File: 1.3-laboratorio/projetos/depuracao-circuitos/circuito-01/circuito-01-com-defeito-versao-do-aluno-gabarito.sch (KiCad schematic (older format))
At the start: 22 parts, among them J1 Conn_01x07_Male, J2 Conn_01x07_Male, J3 Conn_01x07_Male, J4 Conn_01x07_Male, J5 Conn_01x07_Male, J6 Conn_01x07_Male, J7 Conn_01x05, J8 Conn_01x05, P1 CONN_01X02, SW1 SW_DIP_x04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

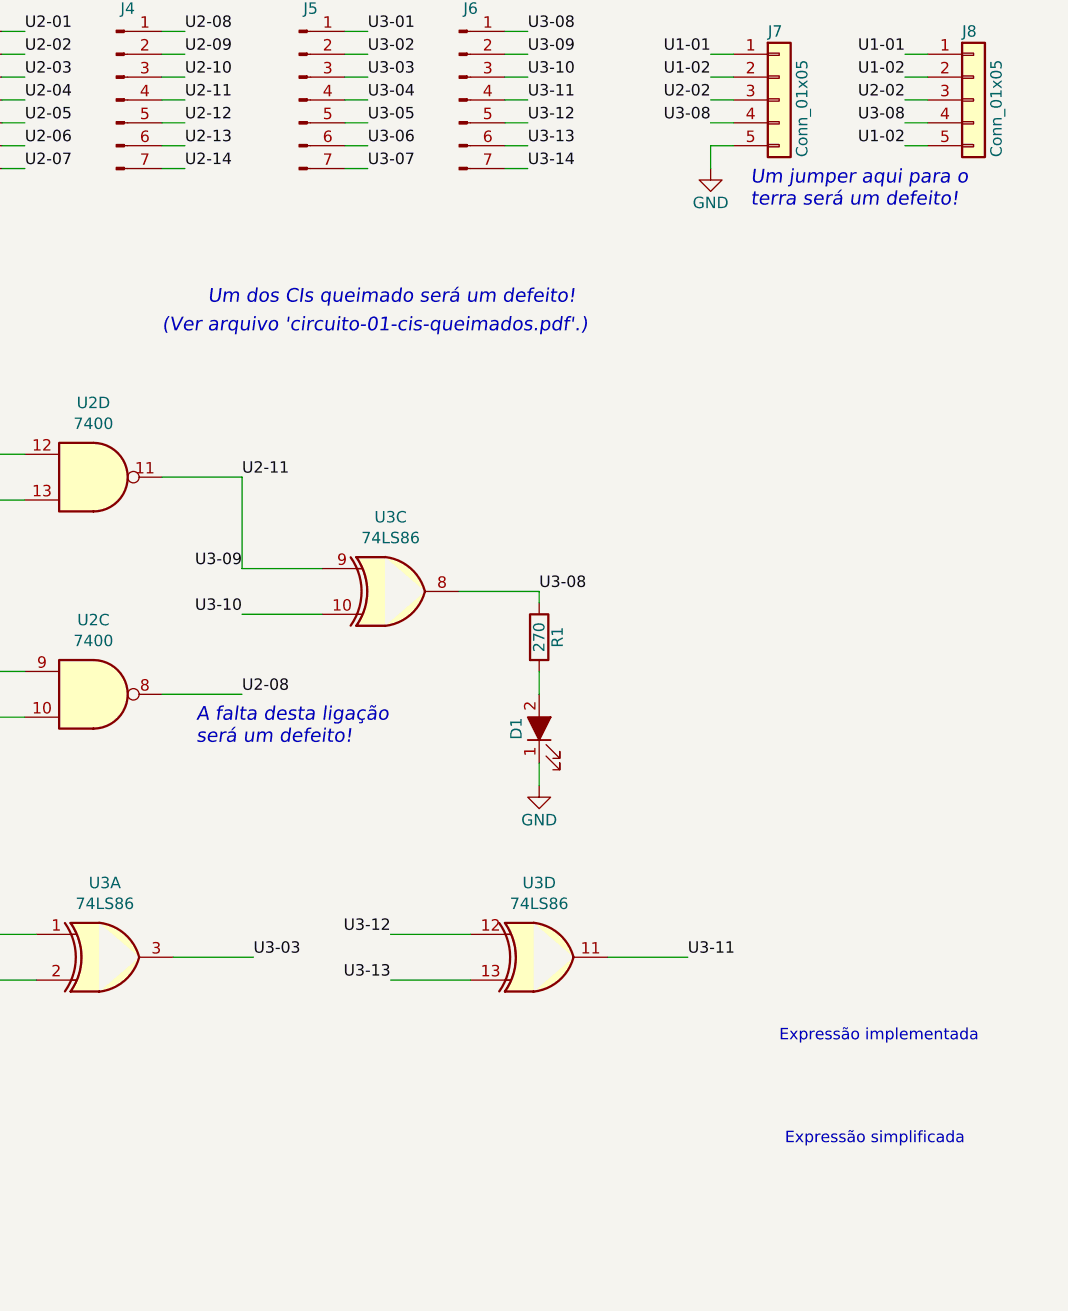
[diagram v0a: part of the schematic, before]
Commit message: Criação do subdiretório 'pdf' e das versões para professor e para aluno do Circuito para Depuração 01.
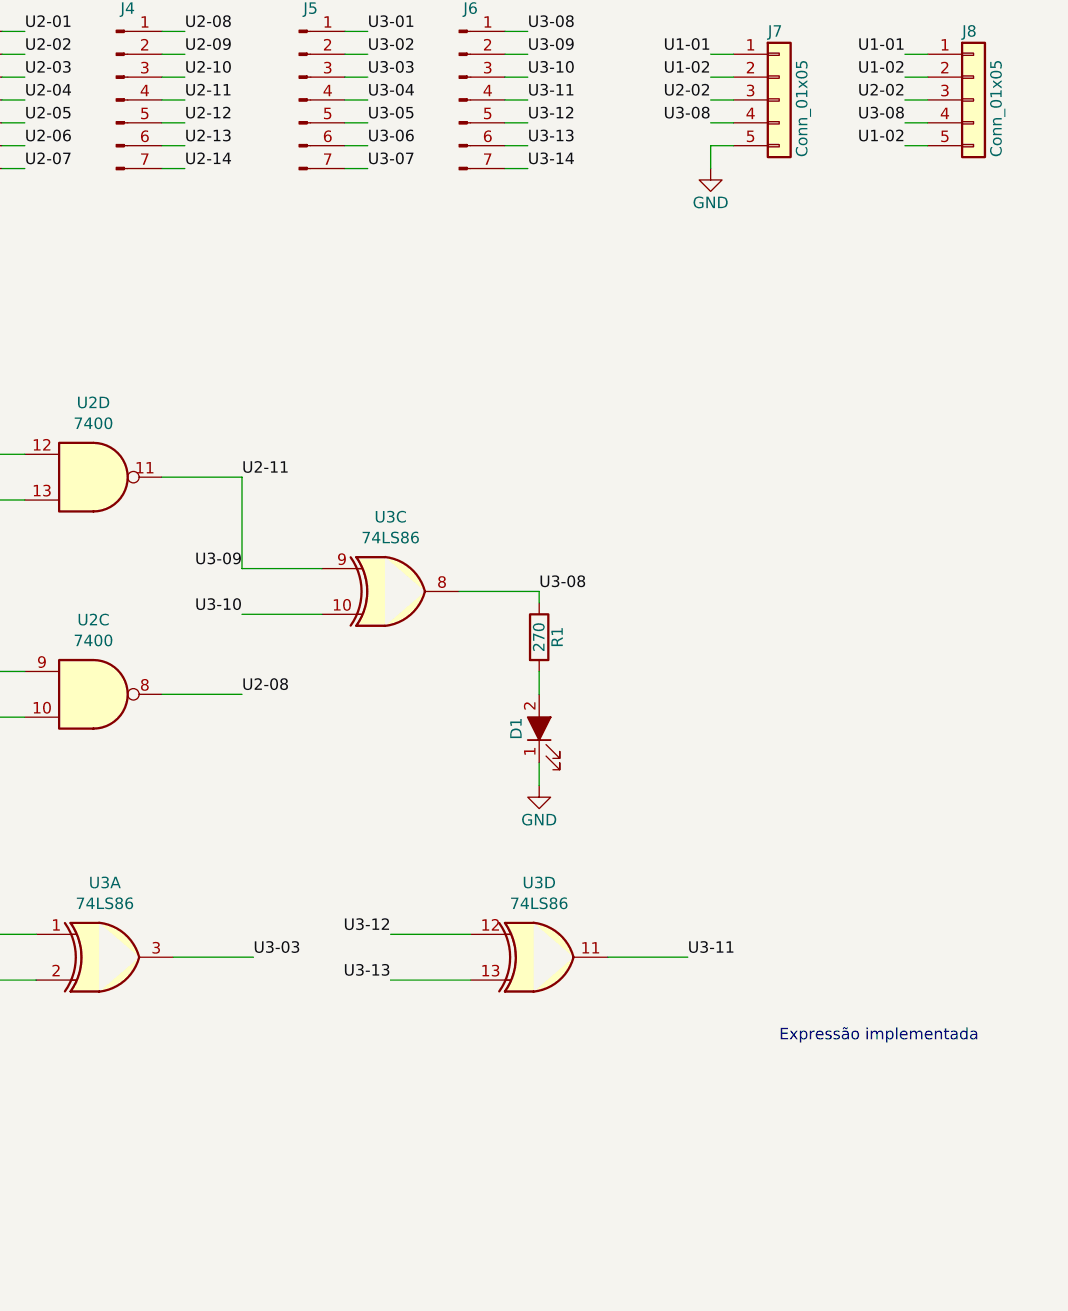
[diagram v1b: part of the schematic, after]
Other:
- note removed: "(Ver arquivo 'circuito-01-cis-queimados.pdf'.)"
- note removed: "A falta desta ligação\nserá um defeito!"
- note removed: "Expressão simplificada"
- note removed: "Um dos CIs queimado será um defeito!"
- note removed: "Um jumper aqui para o\nterra será um defeito!"
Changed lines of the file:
@@
 Comment2 "Com defeitos propositais."
 Comment3 ""
-Comment4 "(Base para a PCI e para gerar as versões do professor e do aluno.)"
+Comment4 "(VERSÃO DO ALUNO - GABARITO)"
 $EndDescr
 $Comp
@@
 Wire Wire Line
 	2050 3450 2300 3450
-Text Notes 9225 1925 0    60   Italic 0
-Um jumper aqui para o\nterra será um defeito!
-Text Notes 6800 4275 0    60   Italic 0
-A falta desta ligação\nserá um defeito!
-Text Notes 6850 2350 0    60   Italic 0
-Um dos CIs queimado será um defeito!
 Wire Wire Line
 	9900 1650 10000 1650
@@
 EndData
 $EndBitmap
-$Bitmap
-Pos 9825 6125
-Scale 1.000000
-Data
-89 50 4E 47 0D 0A 1A 0A 00 00 00 0D 49 48 44 52 00 00 00 CC 00 00 00 2F 08 02 00 00 00 20 90 B2
-89 00 00 00 03 73 42 49 54 08 08 08 DB E1 4F E0 00 00 0B 0C 49 44 41 54 78 9C ED 9B 7D 4C 13 F7
-1F C7 3F ED AE 82 4C 79 52 64 22 62 05 5D 5C 83 E0 44 A9 50 1F 20 46 29 A0 82 D9 E6 A6 89 64 A8
-34 73 6A 1C C6 87 19 74 A0 84 3D 24 84 36 9A FD 33 D1 49 08 83 2D 8A 1A 2D 81 29 3E 41 A7 A0 62
-16 8D 1A 85 02 0E 1C 5A DA 6A 6B E1 DA 5E EF F6 C7 6D AC E9 5D CB 5D CB C1 CF DF EE F5 E7 F7 F3
-7D 78 03 EF FB 7E 3E DF EF 1D 02 82 20 80 87 87 4B 84 63 2D 80 E7 FF 1F DE 64 3C 9C C3 9B 8C 87
-73 78 93 F1 70 0E 6F 32 1E CE E1 4D C6 C3 39 BC C9 78 38 87 37 19 0F E7 F0 26 E3 E1 1C DE 64 3C
-9C F3 86 99 AC A8 A8 48 F0 DF A6 A8 A8 68 AC FF 08 AC 11 F0 EF 2E 79 B8 E6 0D DB C9 78 DE 44 10
-86 FD AC 56 6B 4B 4B 4B 6F 6F EF A4 49 93 64 32 D9 DB 6F BF 0D 00 76 BB BD A7 A7 67 E6 CC 99 5C
-2A F4 9E 9A 9A 9A E9 D3 A7 CB 64 B2 B1 16 F2 5F 67 F8 74 89 E3 78 59 59 59 75 75 B5 54 2A 95 48
-24 9D 9D 9D 4D 4D 4D 9F 7D F6 D9 A6 4D 9B B6 6E DD 9A 96 96 96 9D 9D 3D 3A 5A 59 D1 D5 D5 25 91
-48 F2 F3 F3 4B 4A 4A C6 5A 8B 5B 8C 46 E3 AA 55 AB 6C 36 1B 6D 14 41 90 77 DE 79 67 E9 D2 A5 B9
-B9 B9 C1 C1 C1 A3 AC CD 19 93 C9 94 91 91 61 B5 5A 69 A3 22 91 28 3A 3A 7A EE DC B9 0A 85 22 24
-24 84 A6 07 E1 91 E7 CF 9F 2F 59 B2 A4 A0 A0 C0 6A B5 0E 35 A2 28 BA 71 E3 C6 BC BC 3C 81 40 D0
-DF DF EF 79 86 B1 22 2B 2B 0B 00 72 73 73 C7 5A C8 30 E0 38 DE DF DF 4F FE 6D 4E 9E 3C 89 E3 38
-D9 8E 61 58 7B 7B 7B 55 55 D5 AC 59 B3 66 CC 98 A1 D1 68 C6 5C A7 C1 60 08 0F 0F 07 80 D3 A7 4F
-0F E9 24 08 C2 6C 36 D7 D7 D7 47 44 44 04 05 05 35 34 34 50 C7 7A 32 19 8E E3 2B 57 AE FC F2 CB
-2F A9 21 BD 5E 1F 14 14 34 77 EE 5C DF D5 73 41 5D 5D DD D4 A9 53 01 20 3D 3D 7D A4 E6 B4 D9 6C
-23 35 95 0B 46 A3 51 28 14 8A 44 22 8B C5 42 8D 5A AD D6 94 94 14 04 41 6E DE BC C9 91 00 86 BC
-7E FD 5A 24 12 4D 98 30 C1 6E B7 53 A3 6D 6D 6D 00 10 1C 1C 4C DD 77 3C 99 4C A5 52 4D 9B 36 CD
-DD 2F 37 2D 2D 6D DB B6 6D 5E 2B E6 0E 14 45 D3 D2 D2 BE FF FE 7B 00 98 37 6F 9E 2F 53 BD 7C F9
-52 A5 52 65 67 67 AF 5D BB 36 2A 2A 2A 3B 3B 3B 23 23 23 3F 3F FF EE DD BB 23 A5 96 20 88 73 E7
-CE 01 C0 E2 C5 8B DD 75 E8 EC EC 0C 08 08 48 4A 4A F2 62 72 87 C3 F1 F1 C7 1F FB A0 EE 5F 1A 1A
-1A 00 40 2E 97 BB EB 10 1D 1D 0D 00 B5 B5 B5 2E ED 9E 4E 97 47 8E 1C 49 49 49 11 89 44 B4 51 B1
-58 BC 6C D9 32 C6 69 7D F4 28 2D 2D DD BE 7D 7B 4C 4C 0C 00 FC F9 E7 9F 5E CF 73 EC D8 B1 F4 F4
-F4 E8 E8 E8 5F 7E F9 A5 B6 B6 36 39 39 B9 A6 A6 46 AD 56 6F D9 B2 45 A9 54 6E DC B8 F1 D5 AB 57
-23 22 F8 EA D5 AB 00 90 92 92 E2 AE 83 58 2C 4E 48 48 B8 71 E3 46 63 63 23 DB C9 07 07 07 4F 9F
-3E ED 83 BA 7F F1 AC 93 CC FB 00 80 20 AE A7 49 B7 26 33 99 4C 5A AD 36 20 20 C0 5D 07 AB D5 BA
-74 E9 52 F6 52 B9 E5 E9 D3 A7 F7 EE DD 5B B5 6A 55 44 44 04 00 E8 74 3A 0C C3 D8 4E 42 10 C4 B6
-6D DB 1E 3E 7C D8 D8 D8 B8 7A F5 6A 97 C7 4C 22 91 54 54 54 7C F4 D1 47 59 59 59 DD DD DD BE 6B
-BE 72 E5 0A 78 34 19 00 C4 C6 C6 02 C0 EF BF FF EE FB 72 5E E3 59 67 4B 4B 8B C9 64 1A 37 6E 1C
-CD D6 E3 6E EB 1B 1C 1C 14 0A 85 91 91 91 26 93 89 B6 C3 98 97 08 B4 6C D8 B0 A1 A3 A3 83 20 08
-F2 A9 02 80 DE DE 5E B6 93 14 16 16 96 95 95 B9 34 7E F2 C9 27 28 8A 3A B7 74 76 76 CA 64 32 B3
-D9 EC 8B 60 83 C1 E0 A1 20 1B A2 B8 B8 18 00 F2 F2 F2 D8 CE FF FA F5 6B 04 41 7C 10 F8 37 66 B3
-19 41 10 77 05 99 D5 6A 8D 8F 8F 07 80 F2 F2 72 6A D4 ED 4E E6 EF EF BF 70 E1 C2 9E 9E 9E E5 CB
-97 D7 D7 D7 53 8F AF 52 A9 D4 BB 07 82 3B 7E FD F5 D7 77 DF 7D 97 AC 0C 26 4D 9A E4 E7 E7 07 EC
-33 E6 DD BB 77 7F FB ED B7 2F BE F8 62 D8 9E 62 B1 58 A1 50 14 16 16 7A A7 96 E4 FA F5 EB 38 8E
-4B A5 52 0F 49 03 00 74 3A 1D 00 98 4C 26 5F D6 F2 05 8D 46 83 61 D8 E2 C5 8B A9 D9 50 A7 D3 AD
-5B B7 EE F1 E3 C7 2A 95 6A F3 E6 CD D4 B1 9E 6A 32 95 4A 35 61 C2 84 5B B7 6E A5 A7 A7 87 84 84
-C8 E5 F2 B2 B2 B2 11 49 10 5C 60 B3 D9 94 4A E5 BE 7D FB 86 5A C8 03 26 5B 93 7D FD F5 D7 3F FE
-F8 A3 40 20 60 D2 39 27 27 E7 E9 D3 A7 CF 9E 3D 63 B5 84 33 C3 16 64 24 F7 EF DF 07 80 C8 C8 48
-AF 17 F2 11 52 A7 54 2A B5 FC C3 F3 E7 CF 2F 5E BC 58 52 52 92 92 92 12 16 16 76 FF FE FD 9D 3B
-77 D2 8E F5 74 E3 BF 68 D1 A2 96 96 96 E2 E2 62 B5 5A 6D 36 9B 1B 1A 1A 1A 1A 1A F6 EF DF 5F 52
-52 B2 7B F7 6E 26 CA 4E 9D 3A A5 50 28 08 36 AF 47 85 42 61 4D 4D CD 8A 15 2B 98 0F 21 29 2B 2B
-FB FC F3 CF FD FD FD 87 5A 22 22 22 BA BA BA 58 99 CC 60 30 F8 F9 F9 4D 9B 36 8D F9 90 DC DC DC
-DA DA DA ED DB B7 B3 D0 EA 04 93 82 8C 20 88 3B 77 EE 00 C0 EC D9 B3 BD 5B C5 77 48 9D 46 A3 B1
-B4 B4 74 A8 D1 6A B5 B6 B7 B7 27 24 24 C8 E5 72 32 81 D0 C3 24 1F DB ED F6 E6 E6 E6 A2 A2 A2 B8
-B8 38 72 54 5D 5D 1D 93 81 38 8E EB F5 FA 7E 36 18 0C 06 E7 8B 3E 86 FC F1 C7 1F D4 83 FA 87 1F
-7E 08 00 87 0E 1D 62 3E CF 99 33 67 68 AB 0A 82 AE 26 23 41 51 F4 83 0F 3E 60 BE 84 33 7A BD 5E
-20 10 0C 5B 90 91 0E 13 08 04 3D 3D 3D 6C 97 18 91 9A 8C 2C C8 02 03 03 31 0C A3 46 2F 5C B8 80
-20 88 5C 2E 77 77 DB C5 E8 DD 25 82 20 32 99 4C 26 93 7D F5 D5 57 05 05 05 DF 7C F3 4D 45 45 45
-7A 7A FA B0 03 05 02 41 68 68 28 93 25 7C 64 D7 AE 5D 32 99 4C AD 56 3B 37 0E 0C 0C 00 CB 74 D9
-D3 D3 83 E3 B8 46 A3 A1 86 74 3A 9D 46 A3 21 EB 3C 17 50 14 65 A9 F7 6F AE 5F BF 4E 10 C4 B0 05
-59 65 65 25 00 24 27 27 7B D8 62 9F 3D 7B 76 E9 D2 25 82 92 34 50 14 C5 71 BC A2 A2 82 3A 44 28
-14 CA E5 F2 B0 B0 B0 61 75 36 37 37 63 18 B6 64 C9 92 B7 DE 7A 8B 1A CD CC CC 5C BF 7E 7D 65 65
-E5 E1 C3 87 C9 03 8A 0B F4 26 7B F1 E2 C5 94 29 53 A8 ED 02 81 E0 F0 E1 C3 2A 95 EA D1 A3 47 C3
-2A 1B 35 1A 1B 1B 31 0C 7B F9 F2 E5 ED DB B7 9D DB C9 CB 0B 56 26 B3 D9 6C 1D 1D 1D 76 BB 9D 1A
-D2 EB F5 AD AD AD B4 B7 86 16 8B 85 A5 E4 BF 61 52 90 61 18 56 5D 5D 0D 00 87 0E 1D F2 D0 AD B3
-B3 93 D6 64 E4 61 F0 D2 A5 4B D4 21 42 A1 30 36 36 96 89 C9 48 9D 1E AE 45 93 93 93 2B 2B 2B CF
-9F 3F 4F 6B 32 9A 74 A9 D5 6A 0B 0B 0B 3D 6C 9E 71 71 71 32 99 8C F5 9E CB 0D 36 9B 4D 2E 97 0F
-0C 0C 50 43 E5 E5 E5 00 90 98 98 C8 7C B6 9F 7E FA A9 AA AA 8A 36 E4 2E 5D 62 18 96 95 95 C5 7C
-09 67 C8 F2 83 34 87 3B BE FB EE 3B F0 E1 FD D8 88 A4 CB C4 C4 44 00 68 6D 6D 75 D7 61 EF DE BD
-00 20 16 8B 69 A3 34 3B D9 D5 AB 57 A3 A2 A2 DC 79 D6 E1 70 74 74 74 30 AC 73 D5 6A F5 C1 83 07
-09 96 85 BF 52 A9 64 7E CD AB 54 2A B7 6E DD 3A 7E FC 78 6A 88 FC 29 58 ED 64 89 89 89 2A 95 6A
-C3 86 0D CC 87 B4 B5 B5 CD 9B 37 8F 79 FF 21 F4 7A FD BD 7B F7 44 22 51 52 52 92 BB 3E 4F 9E 3C
-29 2C 2C 8C 8C 8C A4 CD 77 A3 83 D9 6C BE 73 E7 CE C4 89 13 E7 CF 9F EF AE 4F 53 53 13 00 A4 A6
-A6 D2 46 E9 4D E6 21 F7 37 37 37 13 04 91 97 97 C7 44 5F 6A 6A 2A 59 47 33 E9 4C 22 14 0A 25 12
-09 C3 CE BD BD BD 6D 6D 6D E4 63 44 85 3C F0 F7 F5 F5 11 04 C1 F0 4A 22 26 26 E6 C9 93 27 28 8A
-3A 9F 52 3D 53 59 59 49 7B 39 34 2C C3 16 64 16 8B 25 27 27 27 20 20 E0 EC D9 B3 4C 92 1A 47 34
-37 37 3B 1C 0E 99 4C 46 5B 90 01 C0 CF 3F FF 7C E3 C6 8D D0 D0 D0 03 07 0E D0 4F 41 DD DC A2 A2
-A2 16 2D 5A 44 BB EF A1 28 FA DE 7B EF 1D 3D 7A 94 F5 86 CB 0D 99 99 99 8F 1F 3F 76 17 35 1A 8D
-E4 CF C8 EA 7B A4 53 A7 4E ED DC B9 93 DA 4E 9B 2E 6F DE BC E9 F5 D1 72 C7 8E 1D 00 70 E0 C0 01
-DA A8 56 AB 95 4A A5 33 66 CC 78 F0 E0 81 77 F3 93 F8 9E 2E F7 EC D9 03 00 DF 7E FB 2D 6D B4 B5
-B5 35 34 34 14 41 90 C6 C6 46 77 33 B8 9A 4C AB D5 02 80 54 2A DD BF 7F BF 4B 48 A7 D3 65 64 64
-E4 E6 E6 7A 71 C5 30 E2 18 8D C6 4F 3F FD D4 DF DF DF 60 30 B8 EB D3 DE DE 4E 9A CC 73 D1 43 65
-CD 9A 35 D4 EF A2 A8 26 33 9B CD 0B 17 2E 24 DF 62 B1 C5 62 B1 90 DF 66 A9 D5 6A E7 76 1C C7 1F
-3D 7A 94 9F 9F 1F 14 14 B4 63 C7 8E 57 AF 5E 79 31 B9 33 3E 9A 6C 70 70 90 4C 6B 4D 4D 4D 2E A1
-F6 F6 F6 82 82 02 04 41 DE 7F FF 7D CF 9F BB B9 9A EC C4 89 13 39 39 39 18 86 ED D9 B3 67 FE FC
-F9 2A 95 AA AE AE EE EC D9 B3 FB F6 ED 9B 33 67 8E BB A2 78 34 C1 71 7C D9 B2 65 21 21 21 81 81
-81 E3 C7 8F 0F 0D 0D 25 33 B8 33 17 2F 5E 8C 8F 8F 0F 0B 0B 0B 0E 0E 0E 0C 0C 0C 0F 0F 5F B0 60
-C1 B5 6B D7 18 2E 61 32 99 E4 72 F9 B9 73 E7 9C 1B 5D 4C D6 DD DD 9D 99 99 E9 E1 F1 75 47 69 69
-69 5C 5C DC D0 97 AE 62 B1 78 C1 3F C4 C6 C6 CE 9C 39 33 29 29 A9 B8 B8 B8 AB AB 8B ED CC B4 78
-6D B2 23 47 8E C4 C7 C7 0F 7D E9 1A 13 13 33 A4 33 21 21 61 F2 E4 C9 E1 E1 E1 72 B9 FC F8 F1 E3
-0E 87 C3 F3 54 AE 9F 5F 5F BE 7C 39 29 29 89 AC A3 FB FA FA CE 9F 3F DF DD DD ED 70 38 24 12 C9
-9A 35 6B 82 82 82 7C 48 EE 6F 12 03 03 03 0A 85 42 20 10 28 95 CA C9 93 27 03 C0 FA F5 EB 4F 9E
-3C E9 E7 E7 E7 70 38 CA CB CB 7F F8 E1 87 E3 C7 8F 7B 57 F2 8F 26 16 8B 25 38 38 98 F6 52 66 D4
-E0 FF 25 CE 13 1A 8D E6 E8 D1 A3 76 BB 7D CE 9C 39 F5 F5 F5 D9 D9 D9 5A AD F6 C5 8B 17 19 19 19
-0A 85 C2 DD 97 76 FF 53 D8 ED F6 E9 D3 A7 F7 F5 F5 8D A1 06 DE 64 C3 83 A2 28 E9 AD C0 C0 C0 A8
-A8 28 72 63 7B 83 B0 D9 6C E3 C6 8D 1B 43 01 BC C9 78 38 87 FF E7 5E 1E CE E1 4D C6 C3 39 BC C9
-78 38 87 37 19 0F E7 F0 26 E3 E1 1C DE 64 3C 9C C3 9B 8C 87 73 78 93 F1 70 0E 6F 32 1E CE F9 0B
-F0 0E 0B EE 7F 42 CC C4 00 00 00 00 49 45 4E 44 AE 42 60 82
-EndData
-$EndBitmap
 Text Notes 9350 5575 0    50   ~ 0
 Expressão implementada
-Text Notes 9375 6025 0    50   ~ 0
-Expressão simplificada
-Text Notes 6650 2475 0    60   Italic 0
-(Ver arquivo 'circuito-01-cis-queimados.pdf'.)
 $EndSCHEMATC

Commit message: Revisão final das versões do esquema elétrico do Circuito para Depuração 01. Correções de identificação de variáveis de entrada realizadas, incluindo as correções nas expressões e Tabela-Verdade.
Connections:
- net U1-02: no longer J3.2 (Pin_2), J7.3 (Pin_3), J8.3 (Pin_3), R4.2, SW1.6, U2.2
- new net U2-02: J3.2 (Pin_2), J7.3 (Pin_3), J8.3 (Pin_3), R4.2, SW1.6, U2.2
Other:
- note added: "Off: 1\nOn: 0"
